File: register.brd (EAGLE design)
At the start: 100 x 80 mm, 28 parts, among them IC1 74AS574N, IC2 74AS574N, IC3 74AC283N, IC4 74AC283N, IC5 74AC283N, IC6 74AC283N, IC7 74AC244N, IC8 74AC244N

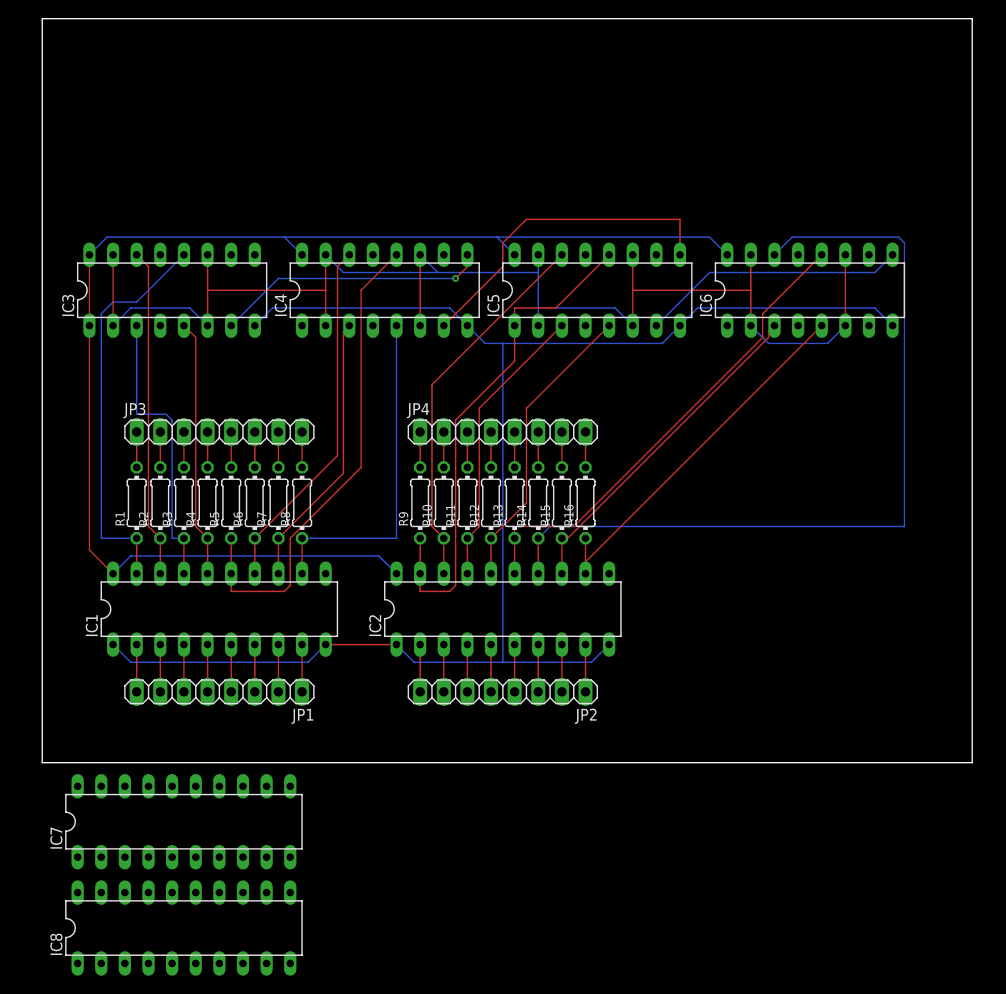
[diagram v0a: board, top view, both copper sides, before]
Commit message: add schematic images
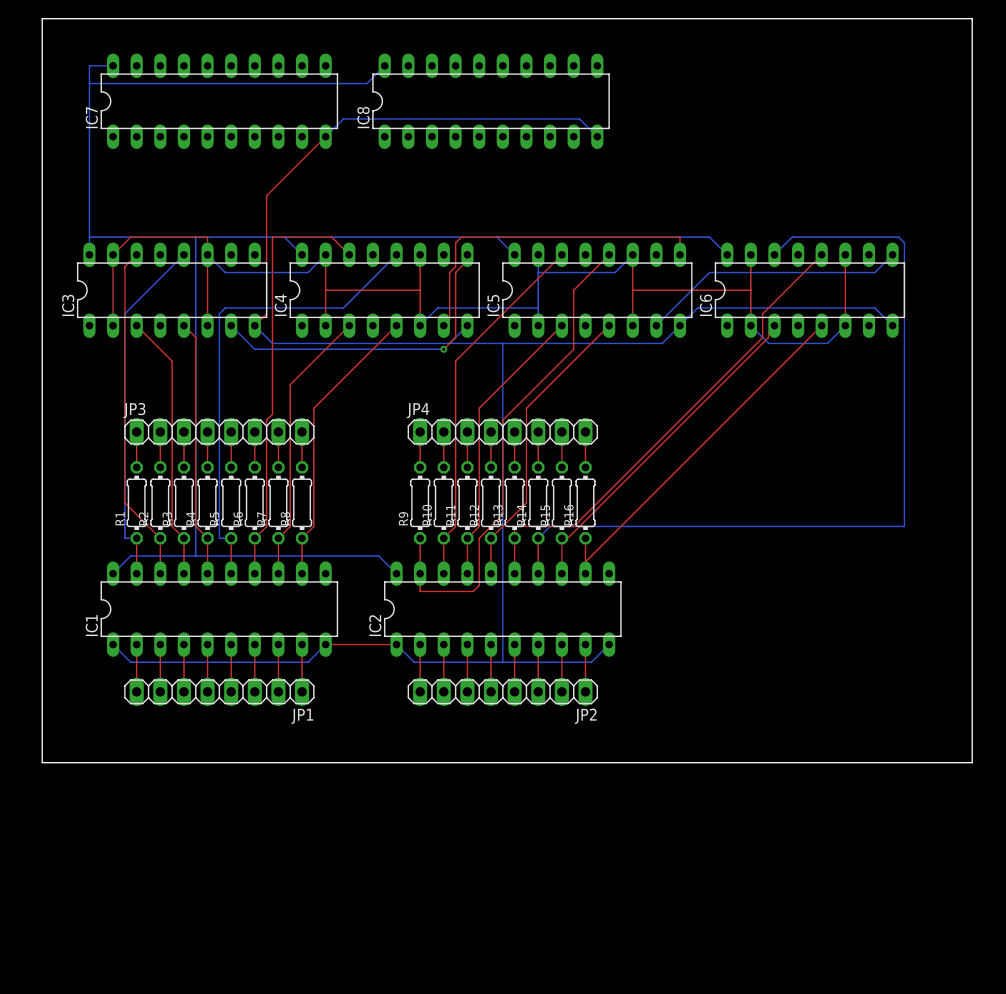
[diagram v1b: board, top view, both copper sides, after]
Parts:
- moved IC8 94.8 mm to (48.3, 71.1)
- moved IC7 77.6 mm to (19.1, 71.1)
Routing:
- net GND: track 164.1 -> 219.5 mm
- net VCC: track 142.9 -> 196.5 mm
- net Q10: track 38.5 -> 46.0 mm
- net Q8: track 36.8 -> 30.9 mm
- net N$17: track 29.3 -> 35.1 mm
- net Q15: track 43.3 -> 38.2 mm
- net Q13: track 31.4 -> 28.8 mm
- net Q11: track 52.6 -> 50.9 mm
- net Q7: track 54.8 -> 53.7 mm
- net Q6: track 40.6 -> 39.6 mm
- net Q14: track 35.3 -> 36.4 mm

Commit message: some work
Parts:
- added D1, D10, D11, D12, D13, D14, D15, D16, D2, D3, D4, D5, D6, D7, D8, D9: (no value), diode:D-7.5
- added IC10: AND(08), 74xx-us:DIL14
- added IC9: NOT(04), 74xx-us:DIL14
- added JP5: (no value), pinhead:1X07
- added JP6, JP7: (no value), pinhead:1X08
- added JP8: (no value), pinhead:1X02
- added R17, R18, R19, R20, R21, R22, R23: 10k, rcl:0204/7
- IC1, IC2: value 74AS574N -> D(574)
- IC3, IC4, IC5, IC6: value 74AC283N -> ADD(283)
- IC7, IC8: value 74AC244N -> BUF(244)
- moved IC8 18.1 mm to (59.7, 57.1)
- moved JP2 16.1 mm to (34.3, 2.54)
- moved IC7 14.2 mm to (16.5, 57.1)
- moved IC2 9.16 mm to (57.1, 11.4)
- moved R11 7.62 mm to (53.3, 27.9)
- moved R12 7.62 mm to (55.9, 27.9)
- moved R13 7.62 mm to (58.4, 27.9)
- moved R16 7.62 mm to (66.0, 27.9)
- moved JP4 7.62 mm to (57.1, 35.6)
- moved R10 7.62 mm to (50.8, 27.9)
- moved R14 7.62 mm to (61.0, 27.9)
- moved R15 7.62 mm to (63.5, 27.9)
- moved R9 7.62 mm to (48.3, 27.9)
- moved IC1 7.18 mm to (14.0, 11.4)
- moved JP1 7.18 mm to (14.0, 2.54)
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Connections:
- removed net LSB: IC2.9, JP2.1
- removed net MSB: IC1.2, JP1.8
- removed net N$10: IC1.8, JP1.2
- removed net N$11: IC1.7, JP1.3
- removed net N$12: IC1.6, JP1.4
- removed net N$13: IC1.5, JP1.5
- removed net N$14: IC1.4, JP1.6
- removed net N$15: IC1.3, JP1.7
- removed net N$8: IC2.2, JP2.8
- removed net N$9: IC1.9, JP1.1
- new net 8BIT: IC1.1, JP5.2, R23.1
- new net B0: IC2.9, IC8.9, JP2.1
- new net B1: IC2.8, IC8.7, JP2.2
- new net B10: IC1.7, IC7.5, JP1.3
- new net B11: IC1.6, IC7.3, JP1.4
- new net B12: IC1.5, IC7.18, JP1.5
- new net B13: IC1.4, IC7.16, JP1.6
- new net B14: IC1.3, IC7.14, JP1.7
- new net B15: IC1.2, IC7.12, JP1.8
- new net B2: IC2.7, IC8.5, JP2.3
- new net B3: IC2.6, IC8.3, JP2.4
- new net B4: IC2.5, IC8.18, JP2.5
- new net B5: IC2.4, IC8.16, JP2.6
- new net B6: IC2.3, IC8.14, JP2.7
- new net B7: IC2.2, IC8.12, JP2.8
- new net B8: IC1.9, IC7.9, JP1.1
- new net B9: IC1.8, IC7.7, JP1.2
- new net CLK: IC10.1, JP5.7, R18.1
- new net CLK2: IC1.11, IC10.6, IC2.11
- new net N$18: IC3.4, IC7.2
- new net N$19: IC3.1, IC7.4
- new net N$20: IC3.13, IC7.6
- new net N$21: IC3.10, IC7.8
- new net N$22: IC4.4, IC7.11
- new net N$23: IC4.1, IC7.13
- new net N$24: IC4.13, IC7.15
- new net N$25: IC4.10, IC7.17
- new net N$26: IC5.4, IC8.2
- new net N$27: IC5.1, IC8.4
- new net N$28: IC5.13, IC8.6
- new net N$29: IC5.10, IC8.8
- new net N$30: IC6.4, IC8.11
- new net N$47: IC6.1, IC8.13
- new net N$48: IC6.13, IC8.15
- new net N$49: IC6.10, IC8.17
- new net RD: IC9.11, JP5.5, R20.1
- new net WE: IC10.2, JP5.6, R19.1
- new net Z: IC9.2, JP5.1
- net DEC: now also JP5.3, R22.1
- net GND: now also IC10.7, IC9.7, JP8.1, R17.1, R18.2, R19.2, R20.2, R21.2, R22.2, R23.2; no longer IC1.1
- net INC: now also JP5.4, R21.1
- net N$2: now also IC10.3, IC10.4, IC9.9; no longer IC2.8, JP2.2
- net N$3: now also D1.C, D10.C, D11.C, D12.C, D13.C, D14.C, D15.C, D16.C, D2.C, D3.C, D4.C, D5.C, D6.C, D7.C, D8.C, D9.C, IC9.1, R17.2; no longer IC2.7, JP2.3
- net N$31: now also JP7.1
- net N$32: now also JP7.2
- net N$33: now also JP7.3
- net N$34: now also JP7.4
- net N$35: now also JP7.5
- net N$36: now also JP7.6
- net N$37: now also JP7.7
- net N$38: now also JP7.8
- net N$39: now also JP6.1
- net N$4: now also IC7.1, IC7.19, IC8.1, IC8.19, IC9.10; no longer IC2.6, JP2.4
- net N$40: now also JP6.2
- net N$41: now also JP6.3
- net N$42: now also JP6.4
- net N$43: now also JP6.5
- net N$44: now also JP6.6
- net N$45: now also JP6.7
- net N$46: now also JP6.8
- net N$5: now also IC10.5, IC9.4; no longer IC2.5, JP2.5
- net N$6: now also IC9.3, IC9.6; no longer IC2.4, JP2.6
- net N$7: now also IC9.5, IC9.8; no longer IC2.3, JP2.7
- net Q0: now also D16.A
- net Q1: now also D15.A
- net Q10: now also D6.A
- net Q11: now also D5.A
- net Q12: now also D4.A
- net Q13: now also D3.A
- net Q14: now also D2.A
- net Q15: now also D1.A
- net Q2: now also D14.A
- net Q3: now also D13.A
- net Q4: now also D12.A
- net Q5: now also D11.A
- net Q6: now also D10.A
- net Q7: now also D9.A
- net Q8: now also D8.A
- net Q9: now also D7.A
- net VCC: now also IC10.14, IC9.14, JP8.2
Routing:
- net N$4: track 5.08 -> 131.1 mm
- net B6: track 0.00 -> 125.5 mm, vias 0 -> 3
- net B7: track 0.00 -> 103.5 mm, vias 0 -> 2
- net B3: track 0.00 -> 100.9 mm, vias 0 -> 3
- net CLK: track 0.00 -> 98.8 mm, vias 0 -> 1
- net B5: track 0.00 -> 96.0 mm, vias 0 -> 2
- net B4: track 0.00 -> 83.9 mm, vias 0 -> 2
- net B15: track 0.00 -> 83.6 mm
- net WE: track 0.00 -> 81.4 mm, vias 0 -> 2
- net VCC: track 196.5 -> 274.6 mm
- net B1: track 0.00 -> 77.0 mm, vias 0 -> 2
- net B2: track 0.00 -> 74.5 mm, vias 0 -> 2
- net 8BIT: track 0.00 -> 74.3 mm
- net B14: track 0.00 -> 73.9 mm
- net N$3: track 5.08 -> 78.3 mm
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- added copper zone on layer 1, net GND
- added copper zone on layer 16, net GND
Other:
- board size 100 x 80 mm -> 92.4 x 68.6 mm

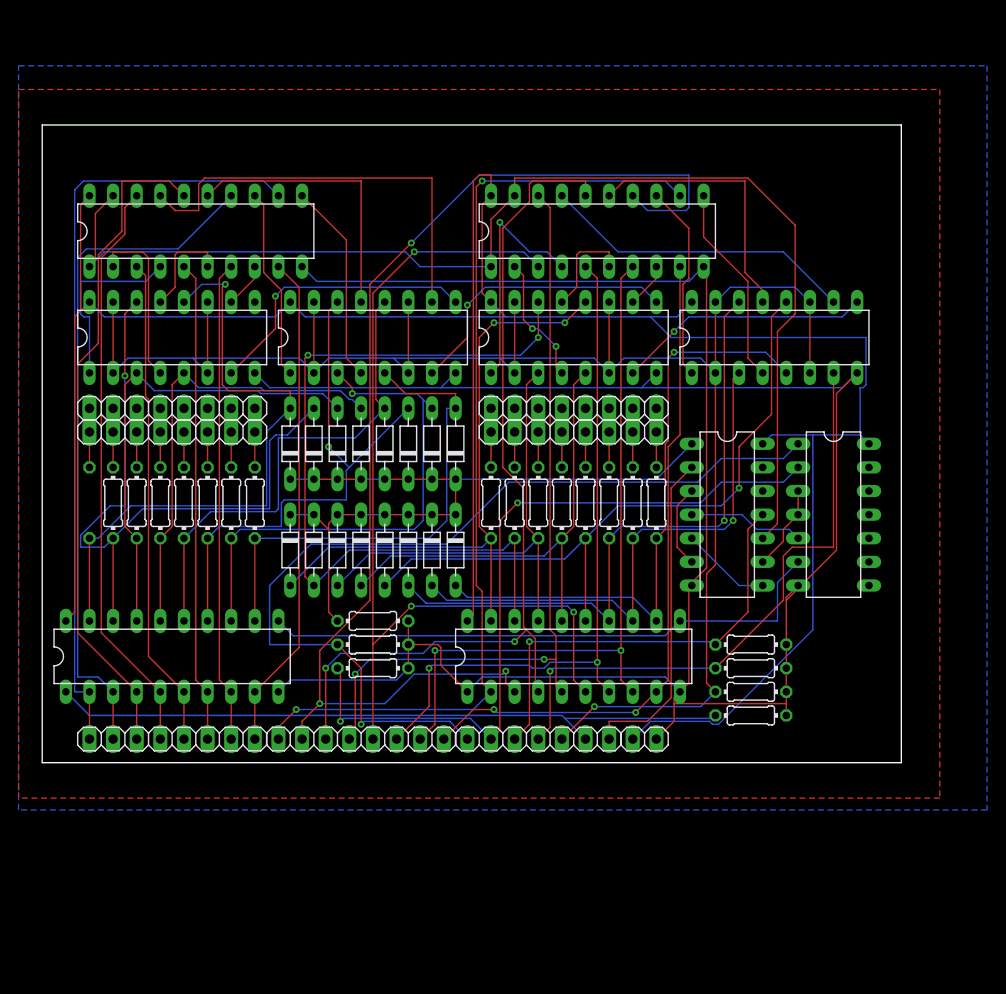
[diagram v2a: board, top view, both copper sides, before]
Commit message: mirror board, some docks
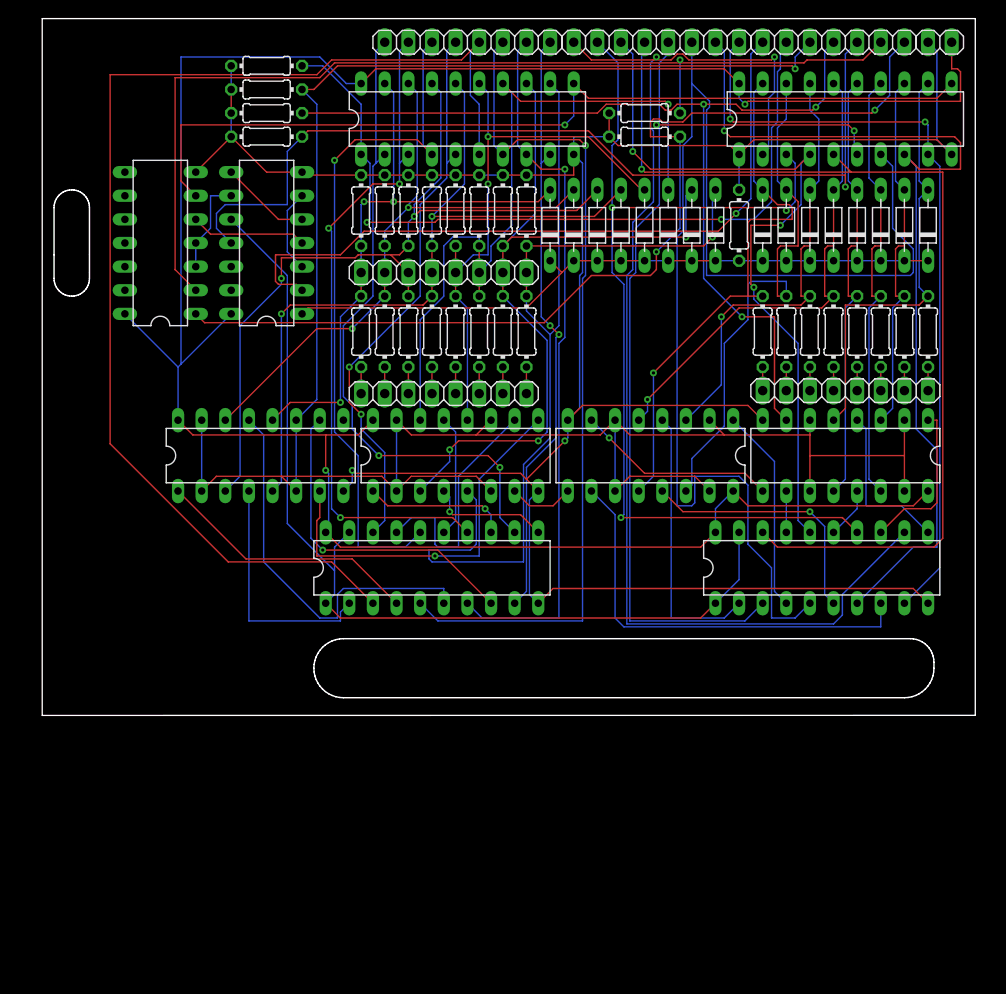
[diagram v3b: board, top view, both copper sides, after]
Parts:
- removed JP7: (no value), pinhead:1X08
- added R24, R25, R26, R27, R28, R29, R30, R31: 10k, rcl:0204/7
- R1, R10, R11, R12, R13, R14, R15, R16, R2, R3, R4, R5, R6, R7, R8, R9: value (none) -> R-LED
- moved R23 87.1 mm to (24.1, 74.9), turned to 180 degrees
- moved R22 83.1 mm to (24.1, 72.4), turned to 180 degrees
- moved JP1 81.4 mm to (45.7, 77.5)
- moved JP2 81.4 mm to (66.0, 77.5)
- moved JP5 81.4 mm to (85.1, 77.5), turned to 0 degrees
- moved JP8 81.4 mm to (96.5, 77.5), turned to 0 degrees
- moved R21 79.2 mm to (24.1, 69.8), turned to 180 degrees
- moved IC10 78.1 mm to (12.7, 55.9), turned to 90 degrees
- moved R20 75.5 mm to (24.1, 67.3), turned to 180 degrees
- moved R19 66.5 mm to (64.8, 69.8), turned to 180 degrees
- moved IC1 65.9 mm to (45.7, 69.2)
- moved IC2 64.7 mm to (86.4, 69.2)
- moved R18 61.9 mm to (64.8, 67.3), turned to 180 degrees
- moved D11 61.6 mm to (82.5, 57.8), turned to 90 degrees
- moved D13 61.6 mm to (87.6, 57.8), turned to 90 degrees
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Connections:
- removed net N$31: JP4.1, JP7.1, R9.2
- removed net N$32: JP4.2, JP7.2, R10.2
- removed net N$33: JP4.3, JP7.3, R11.2
- removed net N$34: JP4.4, JP7.4, R12.2
- removed net N$35: JP4.5, JP7.5, R13.2
- removed net N$36: JP4.6, JP7.6, R14.2
- removed net N$37: JP4.7, JP7.7, R15.2
- removed net N$38: JP4.8, JP7.8, R16.2
- removed net N$39: JP3.1, JP6.1, R1.2
- removed net N$40: JP3.2, JP6.2, R2.2
- removed net N$41: JP3.3, JP6.3, R3.2
- removed net N$42: JP3.4, JP6.4, R4.2
- removed net N$43: JP3.5, JP6.5, R5.2
- removed net N$44: JP3.6, JP6.6, R6.2
- removed net N$45: JP3.7, JP6.7, R7.2
- removed net N$46: JP3.8, JP6.8, R8.2
- new net L0: JP4.8, R16.2
- new net L1: JP4.7, R15.2
- new net L10: JP3.6, R6.2
- new net L11: JP3.5, R5.2
- new net L12: JP3.4, R4.2
- new net L13: JP3.3, R3.2
- new net L14: JP3.2, R2.2
- new net L15: JP3.1, R1.2
- new net L2: JP4.6, R14.2
- new net L3: JP4.5, R13.2
- new net L4: JP4.4, R12.2
- new net L5: JP4.3, R11.2
- new net L6: JP4.2, R10.2
- new net L7: JP4.1, R9.2
- new net L8: JP3.8, R8.2
- new net L9: JP3.7, R7.2
- net GND: now also R24.1, R25.1, R26.1, R27.1, R28.1, R29.1, R30.1, R31.1
- net Q10: now also JP6.6, R26.2
- net Q11: now also JP6.5, R27.2
- net Q12: now also JP6.4, R28.2
- net Q13: now also JP6.3, R29.2
- net Q14: now also JP6.2, R30.2
- net Q15: now also JP6.1, R31.2
- net Q8: now also JP6.8, R24.2
- net Q9: now also JP6.7, R25.2
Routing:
- net B11: track 52.9 -> 129.0 mm
- net B2: track 74.5 -> 139.7 mm, vias 2 -> 0
- net Q8: track 53.5 -> 112.3 mm, vias 0 -> 1
- net RD: track 47.3 -> 97.8 mm
- net DEC: track 201.6 -> 249.1 mm
- net Z: track 35.3 -> 77.1 mm, vias 0 -> 1
- net N$29: track 4.86 -> 46.2 mm
- net B10: track 51.9 -> 92.2 mm, vias 0 -> 1
- net INC: track 65.4 -> 104.0 mm, vias 1 -> 3
- net Q13: track 50.9 -> 87.2 mm, vias 0 -> 2
- net Q12: track 48.4 -> 82.6 mm, vias 0 -> 2
- net CLK2: track 62.2 -> 96.3 mm, vias 0 -> 1
- net N$20: track 10.9 -> 42.2 mm
- net N$21: track 4.86 -> 35.4 mm, vias 0 -> 1
- net N$49: track 33.9 -> 4.45 mm
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- removed copper zone on layer 1, net GND
- removed copper zone on layer 16, net GND
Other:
- board size 92.4 x 68.6 mm -> 100.3 x 74.9 mm
